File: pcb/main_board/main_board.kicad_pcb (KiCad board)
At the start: 2 copper layers, 93 x 75 mm, 71 parts, among them J1 USB_C_Receptacle_USB2.0, J10 Conn_01x04, J11 Conn_01x04, J12 Conn_01x04, J13 Conn_01x04, J14 Conn_01x04, J15 Conn_01x04, J16 Conn_01x03, J2 Jack-DC, J3 Conn_01x02, J4 Conn_02x05_Counter_Clockwise, J5 Conn_01x04, J6 Conn_01x02, J7 Conn_01x02, J8 Conn_02x05_Odd_Even, J9 Conn_01x04, Q1 2SC3325-Y,LF, Q2 2SC3325-Y,LF, SW3 SW_DIP_x03, SW4 SW_DIP_x03, SW5 SW_DIP_x03, U1 ESP32-WROOM-32U, U2 CH340K, U3 AP2204R-5.0, U4 STM32F303K8Tx, U5 A4988_STEPPER_MOTOR_DRIVER_CA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, U6 A4988_STEPPER_MOTOR_DRIVER_CA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, U7 A4988_STEPPER_MOTOR_DRIVER_CA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, Y1 Crystal_GND2

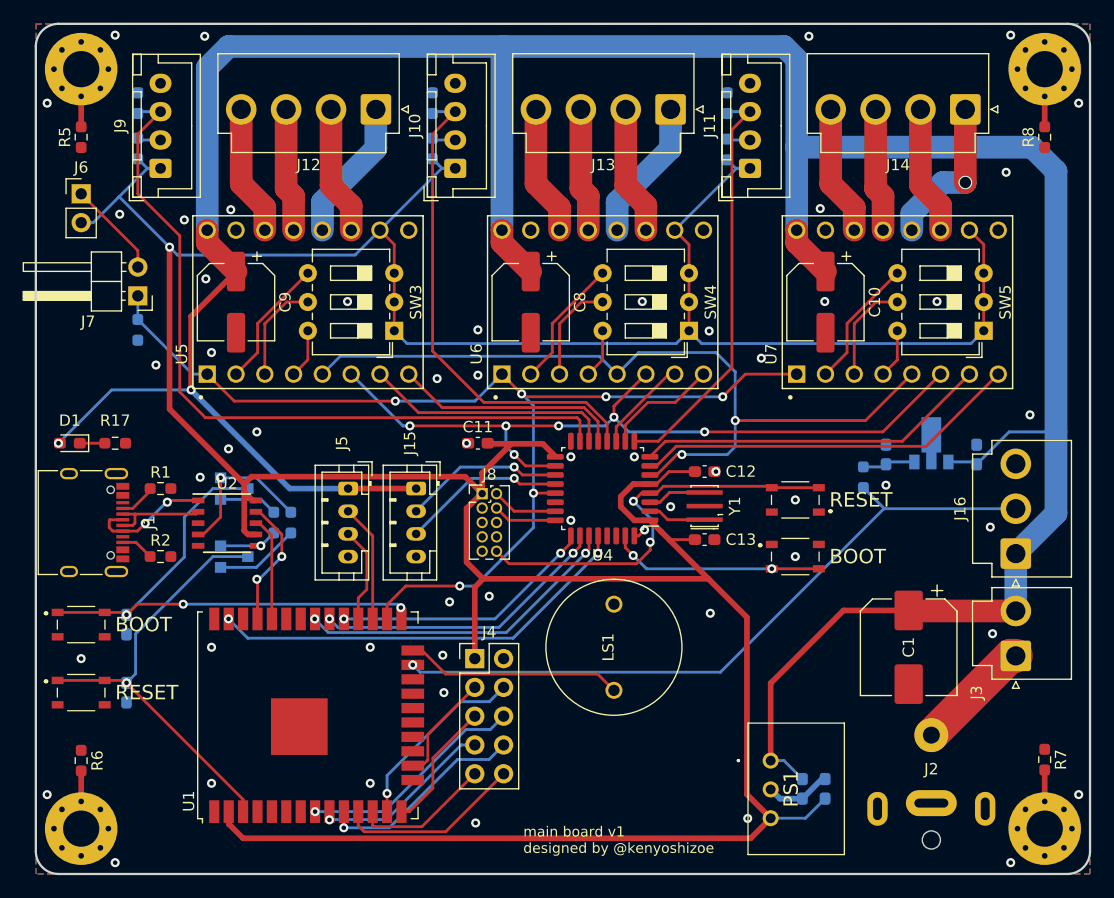
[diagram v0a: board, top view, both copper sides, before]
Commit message: 🐛 minor fix
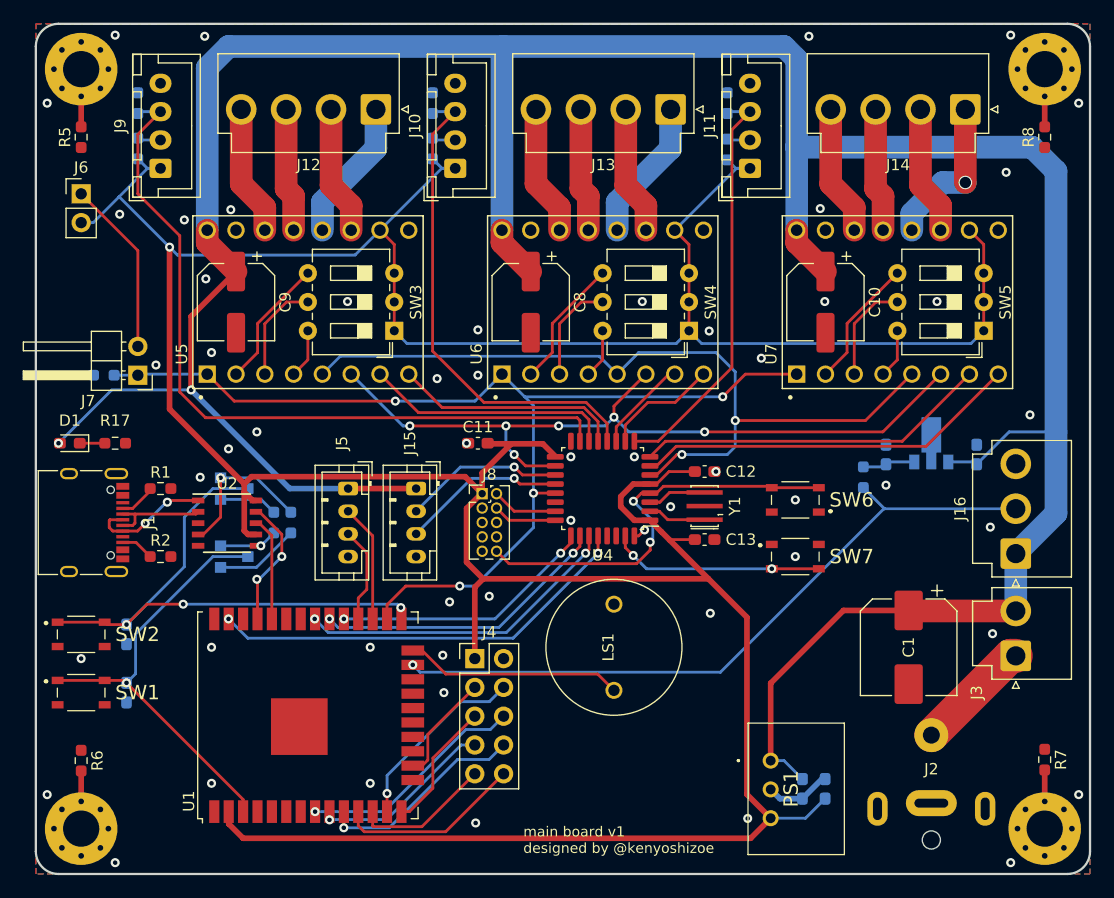
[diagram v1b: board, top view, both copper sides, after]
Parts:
- R1, R2: value 22 -> 5.1k
- moved J7 7.00 mm to (69.0, 91.0)
- moved R9 5.00 mm to (66.0, 91.0), turned to 180 degrees
- moved C5 0.86 mm to (68.0, 113.9)
- moved SW2 0.86 mm to (64.0, 113.9)
- renumbered RESET to SW1, BOOT to SW2, RESET to SW6, BOOT to SW7
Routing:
- net Net-(J6-Pad1): track 8.53 -> 15.5 mm
- net ~{EMG}: track 97.0 -> 94.6 mm, vias 6 -> 4
- net IO0: track 49.3 -> 50.5 mm
